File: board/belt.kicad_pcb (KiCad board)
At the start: 2 copper layers, 48.3 x 73.6 mm, 33 parts, among them J1 USB_B_Micro, J2 USB_B_Micro, J3 USB_B_Micro, J4 USB_B_Micro, P1 10K, P2 10K, Q1 BSS138, Q2 BSS138, SW1 SW_SPDT, SW2 SW_Push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

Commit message: sign it
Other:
- board text added: "by opal"
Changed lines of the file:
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@@
-(kicad_pcb (version 20171130) (host pcbnew "(5.1.2-1)-1")
+(kicad_pcb (version 20171130) (host pcbnew "(5.1.5-0-10_14)")
   (general
     (thickness 1.6)
-    (drawings 31)
+    (drawings 42)
     (tracks 287)
     (zones 0)
@@
     (solder_mask_min_width 0.25)
     (aux_axis_origin 0 0)
-    (visible_elements FFFFF77F)
+    (visible_elements FFFFFF7F)
     (pcbplotparams
       (layerselection 0x010fc_ffffffff)
@@
     )
   )
+  (gr_circle (center 163.576 122.682) (end 163.703 123.571) (layer F.SilkS) (width 0.12))
+  (gr_line (start 162.814 119.38) (end 163.576 118.999) (layer F.SilkS) (width 0.12))
+  (gr_line (start 164.338 121.666) (end 164.338 119.38) (layer F.SilkS) (width 0.12))
+  (gr_line (start 164.338 119.38) (end 163.576 118.999) (layer F.SilkS) (width 0.12))
+  (gr_line (start 162.814 121.666) (end 162.814 119.38) (layer F.SilkS) (width 0.12))
+  (gr_text "by opal" (at 165.862 122.555 90) (layer F.SilkS)
+    (effects (font (size 1 1) (thickness 0.15)))
+  )
+  (gr_line (start 164.338 125.984) (end 163.576 126.365) (layer F.SilkS) (width 0.12))
+  (gr_line (start 164.338 123.698) (end 164.338 125.984) (layer F.SilkS) (width 0.12))
+  (gr_line (start 162.814 125.984) (end 163.576 126.365) (layer F.SilkS) (width 0.12))
+  (gr_line (start 162.814 123.698) (end 162.814 125.984) (layer F.SilkS) (width 0.12))
+  (gr_circle (center 163.576 122.682) (end 164.846 122.555) (layer F.SilkS) (width 0.12))
   (gr_circle (center 164.465 73.66) (end 164.592 74.803) (layer F.SilkS) (width 0.12))
   (gr_circle (center 164.465 73.66) (end 165.237511 73.66) (layer F.SilkS) (width 0.1))

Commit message: flip entire board outline vertically which somehow fixed OSHPark thinking the outline wasn't contiguous
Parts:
- REF** (x4): moved to B.Cu
- moved REF** 69.2 mm to (161.3, 138.4)
- moved REF** 69.2 mm to (125.7, 138.4)
- moved REF** 69.2 mm to (125.7, 69.2)
- moved REF** 69.2 mm to (161.3, 69.2)

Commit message: move power switch footprint in a project-specific library and make it a bit more detailed
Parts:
- SW1: footprint Extra SMD Components:Button_Switch_SPDT_GH36P010001 -> belt:Button_Switch_SPDT_GH36P010001

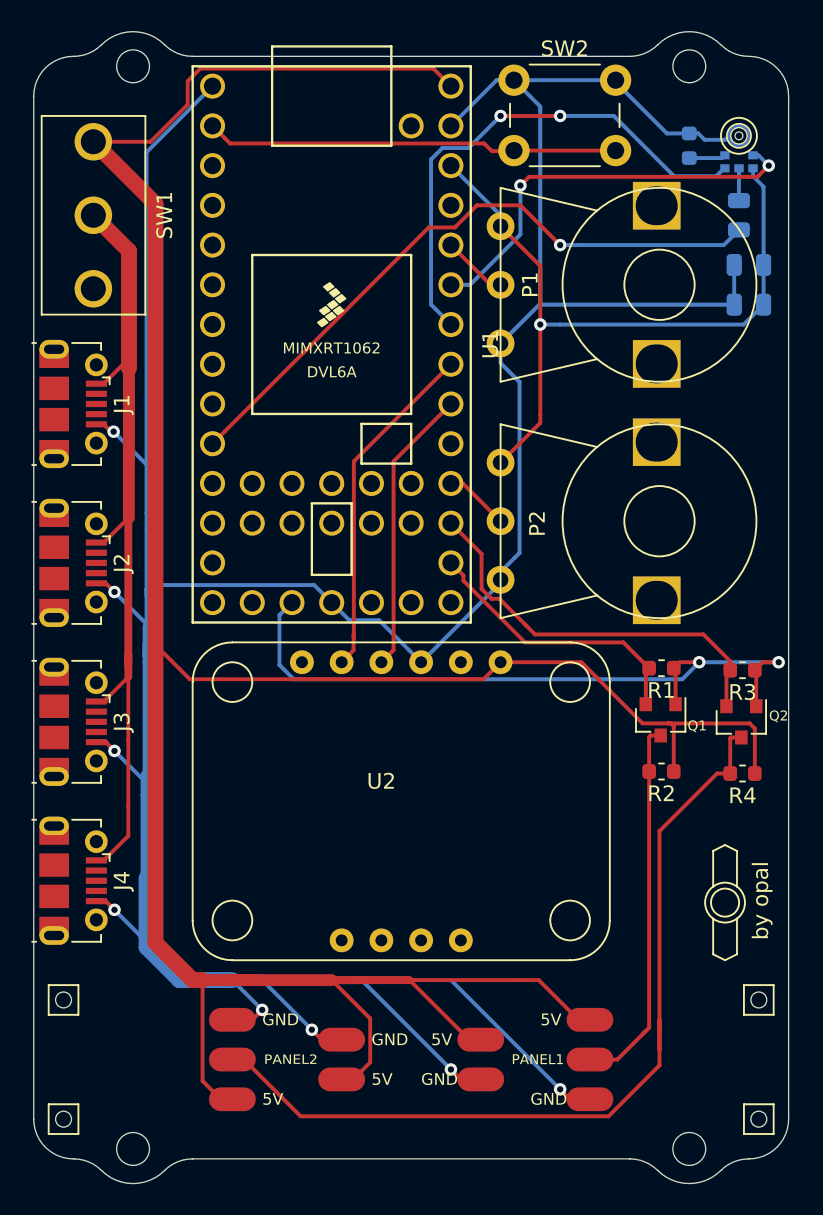
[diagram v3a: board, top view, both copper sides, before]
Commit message: move several belt footprints into local belt footprint library; fix footprints for power switch and BNO055 which had through-holes that were too small
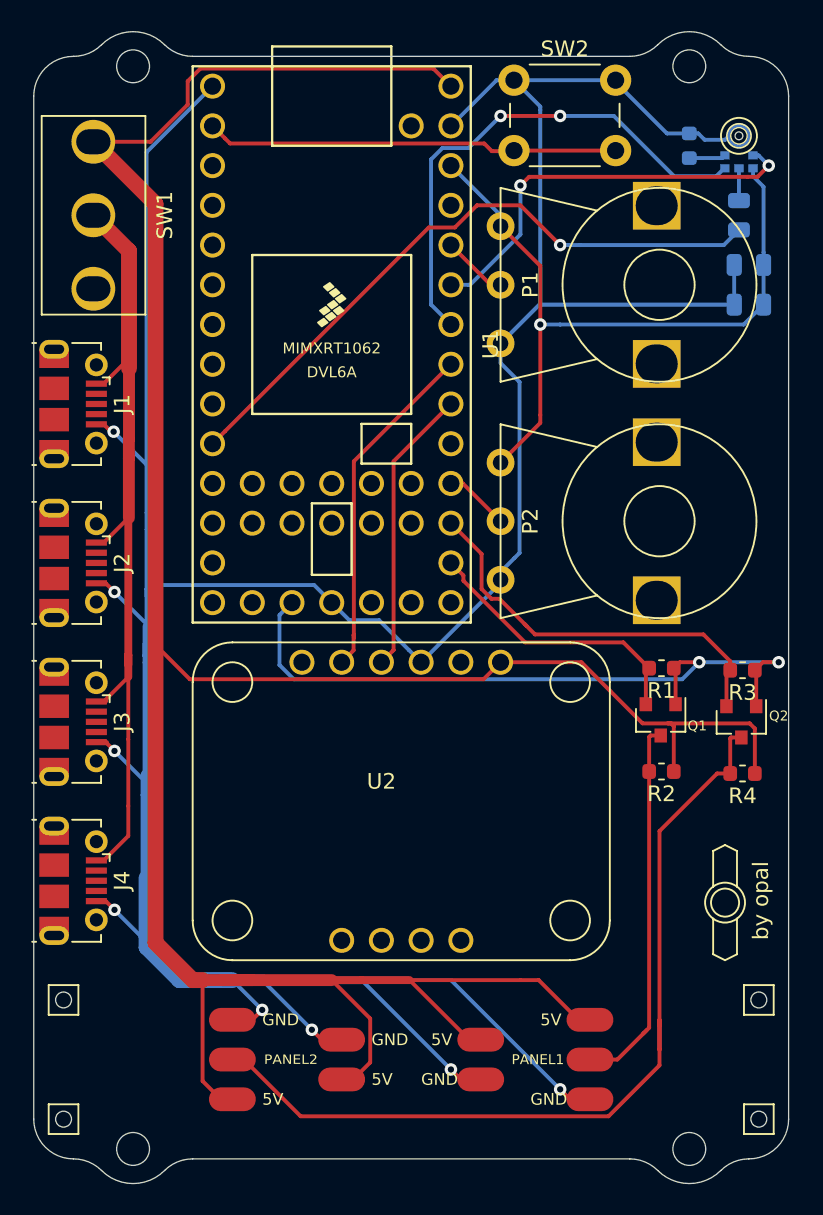
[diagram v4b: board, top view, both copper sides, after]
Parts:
- P1, P2: footprint Potentiometer_THT:PDB12-H -> belt:PDB12-H
- PANEL1, PANEL2: footprint Pad_SMD:Pad_SMD_01x03 -> belt:Pad_SMD_01x03
- PANEL_PWR1, PANEL_PWR2: footprint Pad_SMD:Pad_SMD_01x02 -> belt:Pad_SMD_01x02
- U1: footprint teensy:Teensy40 -> belt:Teensy40
- U2: footprint BreakoutBoards:Adafruit_BNO055 -> belt:Adafruit_BNO055
